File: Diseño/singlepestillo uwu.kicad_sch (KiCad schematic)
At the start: 17 parts, among them J1 MAX98357A, J2 Conn_01x03_Pin, J3 Screw_Terminal_01x03, J5 Screw_Terminal_01x02, J9 Screw_Terminal_01x03, K3 G6AU, Q6 MMBT2222A, U3 EL817, U5 L7805, U6 ESP32DevKitv1

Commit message: avance pcb armado
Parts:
- U5: footprint MacroLib:TO-220-3_Vertical -> Package_TO_SOT_THT:TO-3P-3_Vertical
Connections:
- net J5 - COM is gone; now on net J3 - COM: J3.3 (Pin_3)
- net J5 - NA is gone; now on net J3 - NA: J3.2 (Pin_2)
- net J5 - NC is gone; now on net J3 - NC: J3.1 (Pin_1)
- net J6 - COM is gone; now on net J4 - COM: J9.2 (Pin_2)
- net J6 - NA is gone; now on net J4 - NA: J9.3 (Pin_3)
- net J6 - NC is gone; now on net J4 - NC: J9.1 (Pin_1)
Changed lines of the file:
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@@
 		)
 	)
-	(global_label "J6 - NC"
+	(global_label "J4 - NC"
 		(shape input)
 		(at 255.778 90.424 180)
@@
 		)
 	)
-	(global_label "J6 - NA"
+	(global_label "J4 - NA"
 		(shape input)
 		(at 255.778 95.504 180)
@@
 		)
 	)
-	(global_label "J6 - COM"
+	(global_label "J4 - COM"
 		(shape input)
 		(at 255.778 92.964 180)
@@
 		)
 	)
-	(global_label "J5 - NA"
+	(global_label "J3 - NA"
 		(shape input)
 		(at 255.778 84.074 180)
@@
 		)
 	)
-	(global_label "J5 - COM"
+	(global_label "J3 - COM"
 		(shape input)
 		(at 255.778 86.614 180)
@@
 		)
 	)
-	(global_label "J5 - NC"
+	(global_label "J3 - NC"
 		(shape input)
 		(at 255.778 81.534 180)
@@
 			)
 		)
-		(property "Footprint" "MacroLib:TO-220-3_Vertical"
+		(property "Footprint" "Package_TO_SOT_THT:TO-3P-3_Vertical"
 			(at 72.263 34.544 0)
 			(effects

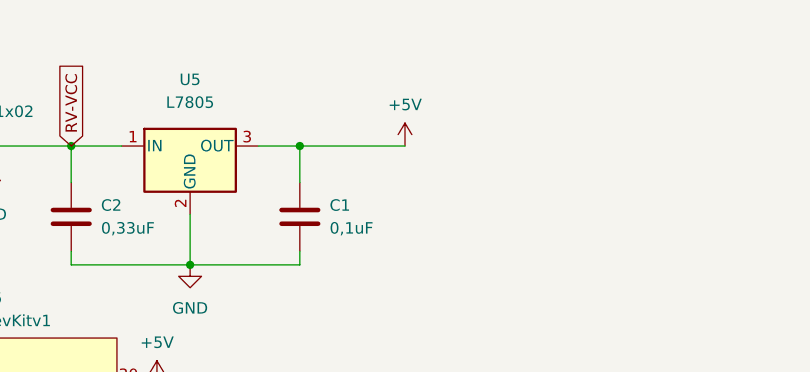
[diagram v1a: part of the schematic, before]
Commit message: correcion pcb y avance codigo
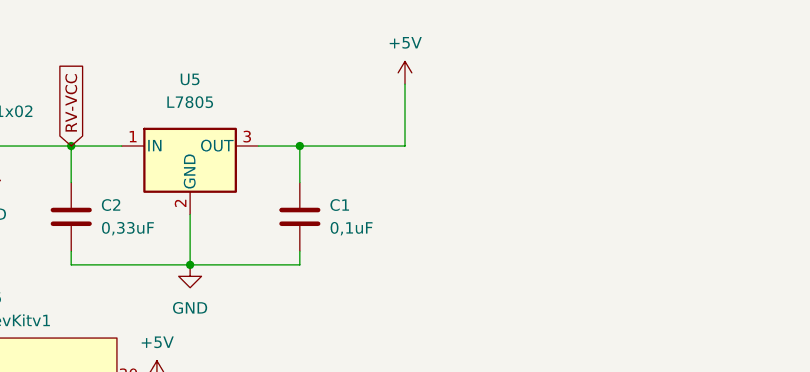
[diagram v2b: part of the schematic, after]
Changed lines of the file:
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@@
+	(wire
+		(pts
+			(xy 95.504 23.876) (xy 95.504 30.734)
+		)
+		(stroke
+			(width 0)
+			(type default)
+		)
+	)
 	(wire
 		(pts
@@
 	(symbol
 		(lib_id "power:+5V")
-		(at 95.504 30.734 0)
+		(at 95.504 23.876 0)
 		(unit 1)
 		(exclude_from_sim no)
@@
 		(fields_autoplaced yes)
 		(property "Reference" "#PWR012"
-			(at 95.504 34.544 0)
+			(at 95.504 27.686 0)
 			(effects
 				(font
@@
 		)
 		(property "Value" "+5V"
-			(at 95.504 26.162 0)
+			(at 95.504 19.304 0)
 			(effects
 				(font
@@
 		)
 		(property "Footprint" ""
-			(at 95.504 30.734 0)
+			(at 95.504 23.876 0)
 			(effects
 				(font
@@
 		)
 		(property "Datasheet" ""
-			(at 95.504 30.734 0)
+			(at 95.504 23.876 0)
 			(effects
 				(font
@@
 		)
 		(property "Description" "Power symbol creates a global label with name \"+5V\""
-			(at 95.504 30.734 0)
-			(effects
-				(font
+			(at 95.504 23.876 0)
+			(effects
+				(font

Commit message: Primer modelo final pcb
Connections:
- net GPIO19: now also J1.3 (Pin_3)
- net GPIO26: no longer names the net of U6.24 (D26)
- net GPIO26: no longer J1.3 (Pin_3)
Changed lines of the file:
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@@
-		)
-	)
-	(global_label "GPIO26"
-		(shape output)
-		(at 66.04 72.39 0)
-		(fields_autoplaced yes)
-		(effects
-			(font
-				(size 1.27 1.27)
-			)
-			(justify left)
-		)
-		(property "Intersheetrefs" "${INTERSHEET_REFS}"
-			(at 75.9195 72.39 0)
-			(effects
-				(font
-					(size 1.27 1.27)
-				)
-				(justify left)
-				(hide yes)
-			)
 		)
 	)
@@
 		)
 	)
-	(global_label "GPIO26"
+	(global_label "GPIO19"
 		(shape input)
 		(at 136.271 88.138 180)

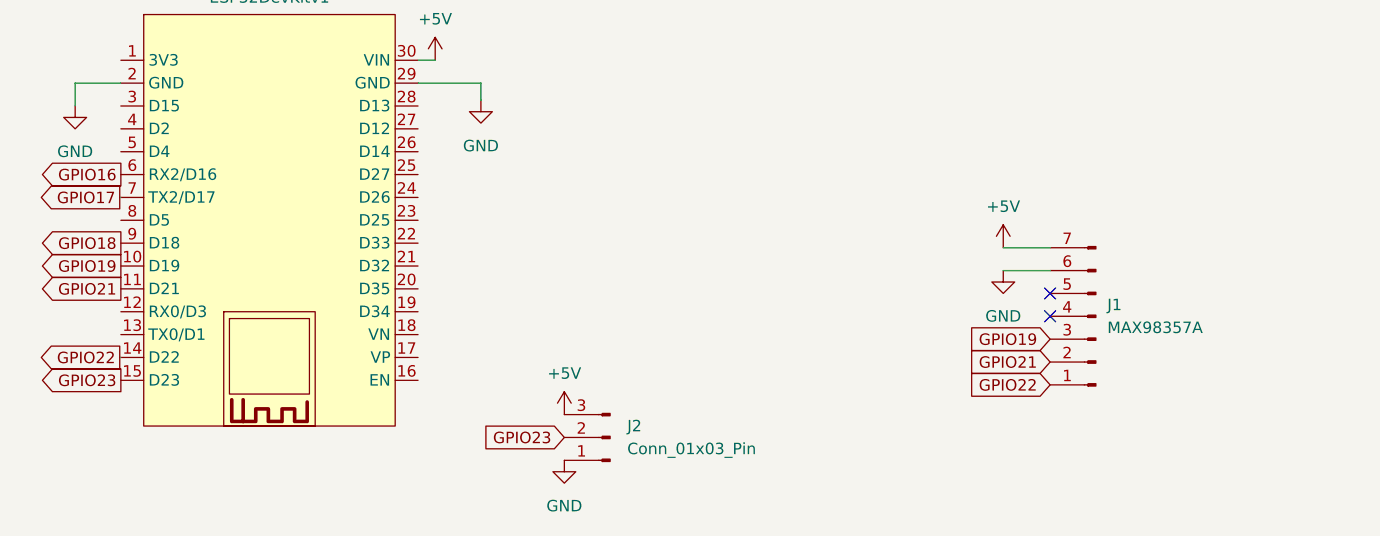
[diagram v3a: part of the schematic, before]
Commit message: Cambios en el amplificador del pcb, programacion actualizada
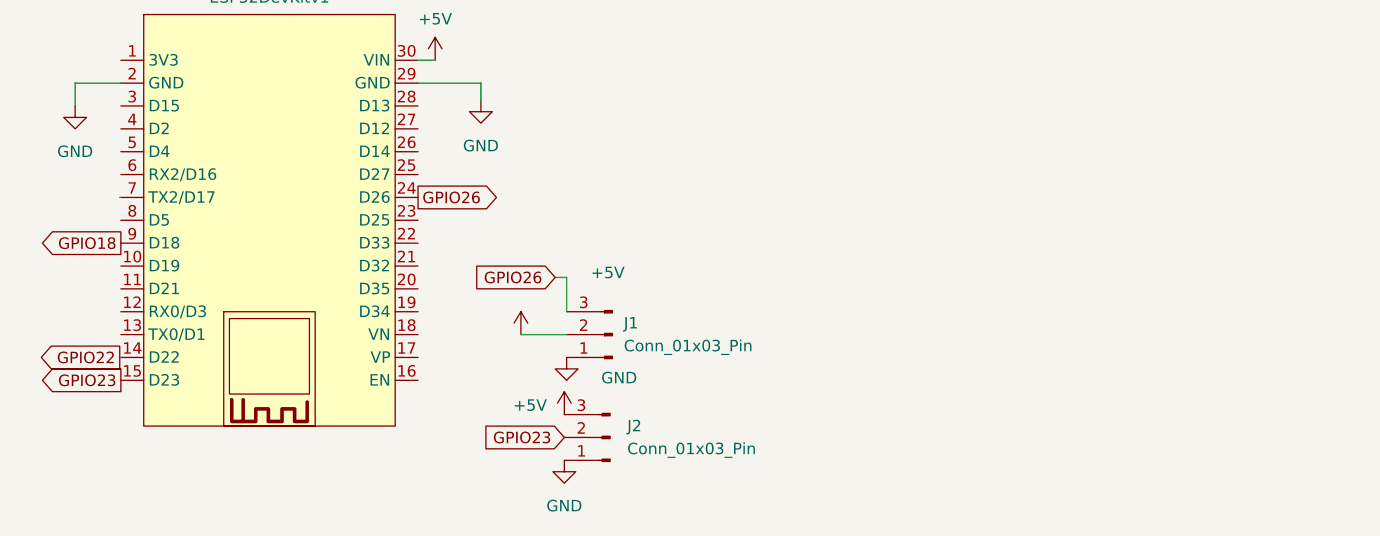
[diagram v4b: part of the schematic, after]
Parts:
- removed J1: MAX98357A, Connector_PinHeader_2.54mm:PinHeader_1x07_P2.54mm_Vertical, symbol Connector:Conn_01x07_Pin
- added J1: Conn_01x03_Pin, Connector_PinHeader_2.54mm:PinHeader_1x03_P2.54mm_Vertical, symbol Connector:Conn_01x03_Pin
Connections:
- net +5V: now also J1.2 (Pin_2)
- net GND: now also J1.1 (Pin_1)
- net GPIO26: now reaches U6.24 (D26)
- net GPIO26: now also J1.3 (Pin_3)
- net GPIO16: no longer names the net of U6.6 (RX2/D16)
- net GPIO17: no longer names the net of U6.7 (TX2/D17)
- net GPIO19: no longer names the net of U6.10 (D19)
- net GPIO21: no longer names the net of U6.11 (D21)
- no-connect marks 2 -> 0
